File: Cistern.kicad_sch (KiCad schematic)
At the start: 16 parts, among them J2 Gauge Stepper, J3 Power Connector, Q1 BD244C, Q2 Gauge Calibration, SW1 WiFi reset, SW2 Water Sensor, U1 ULN2003A, U3 Boost Converter (5->20 V)

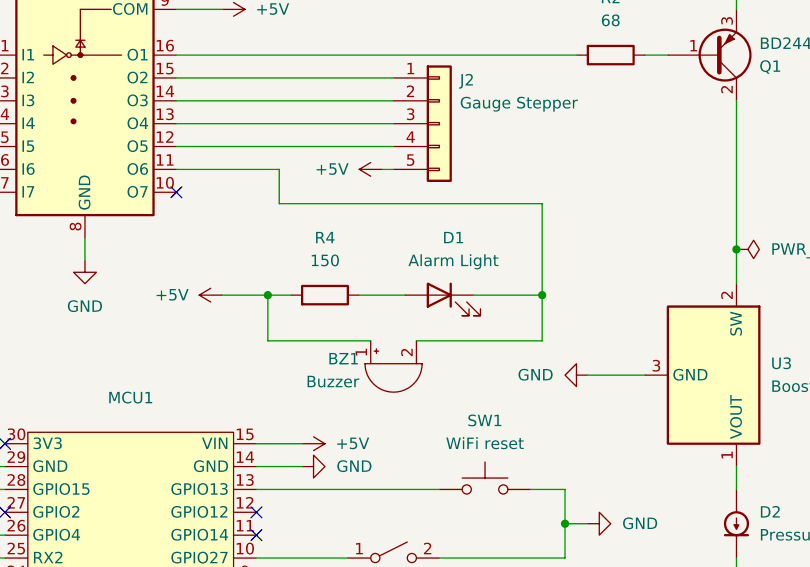
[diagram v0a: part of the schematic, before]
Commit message: Improving design some more, fixing custom footprints
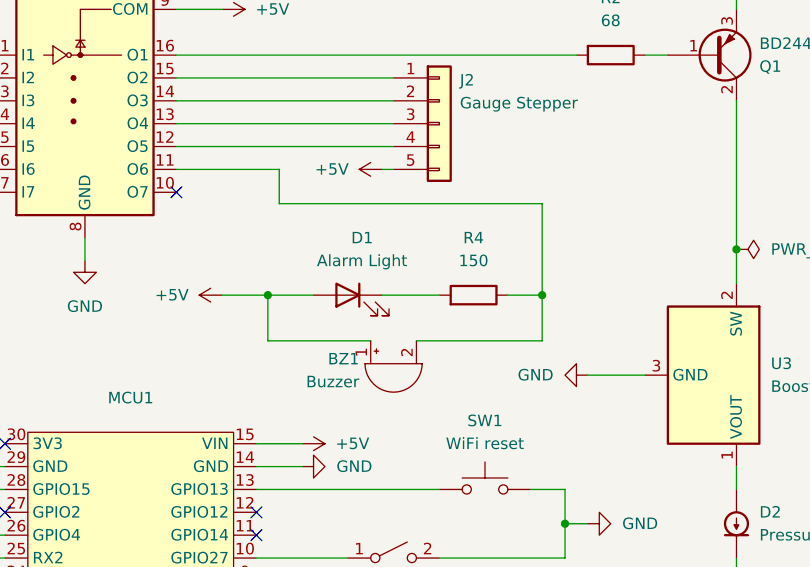
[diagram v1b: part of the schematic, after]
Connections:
- net +5V: now also D1.2 (A); no longer R4.2
- net at BZ1.2 (-), U1.11 (O6): now also R4.1; no longer D1.1 (K)
- new net: D1.1 (K), R4.2
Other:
- moved on the sheet: D1, R4
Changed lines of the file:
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@@
+	)
+	(junction
+		(at 59.69 160.02)
+		(diameter 0)
+		(color 0 0 0 0)
+	)
+	(junction
+		(at 228.6 110.49)
+		(diameter 0)
+		(color 0 0 0 0)
 	)
 	(junction
@@
 	)
 	(junction
-		(at 59.69 160.02)
-		(diameter 0)
-		(color 0 0 0 0)
-	)
-	(junction
-		(at 228.6 110.49)
-		(diameter 0)
-		(color 0 0 0 0)
-	)
-	(junction
 		(at 223.52 120.65)
 		(diameter 0)
@@
 	(wire
 		(pts
-			(xy 207.01 78.74) (xy 207.01 73.66)
-		)
-		(stroke
-			(width 0)
-			(type default)
-		)
-	)
-	(wire
-		(pts
 			(xy 133.35 95.25) (xy 147.32 95.25)
 		)
@@
 	(wire
 		(pts
+			(xy 176.53 73.66) (xy 181.61 73.66)
+		)
+		(stroke
+			(width 0)
+			(type default)
+		)
+	)
+	(wire
+		(pts
 			(xy 209.55 99.06) (xy 212.09 99.06)
 		)
@@
 	(wire
 		(pts
-			(xy 199.39 73.66) (xy 207.01 73.66)
-		)
-		(stroke
-			(width 0)
-			(type default)
-		)
-	)
-	(wire
-		(pts
 			(xy 228.6 120.65) (xy 228.6 119.38)
 		)
@@
 	(wire
 		(pts
-			(xy 176.53 78.74) (xy 176.53 73.66)
+			(xy 176.53 73.66) (xy 176.53 78.74)
 		)
 		(stroke
@@
 	(wire
 		(pts
+			(xy 207.01 73.66) (xy 207.01 78.74)
+		)
+		(stroke
+			(width 0)
+			(type default)
+		)
+	)
+	(wire
+		(pts
 			(xy 187.96 78.74) (xy 176.53 78.74)
 		)
@@
 	(wire
 		(pts
+			(xy 203.2 73.66) (xy 207.01 73.66)
+		)
+		(stroke
+			(width 0)
+			(type default)
+		)
+	)
+	(wire
+		(pts
 			(xy 134.62 123.19) (xy 147.32 123.19)
 		)
@@
 	(wire
 		(pts
-			(xy 176.53 73.66) (xy 179.07 73.66)
-		)
-		(stroke
-			(width 0)
-			(type default)
-		)
-	)
-	(wire
-		(pts
 			(xy 59.69 156.21) (xy 59.69 160.02)
 		)
@@
 	(wire
 		(pts
+			(xy 189.23 73.66) (xy 195.58 73.66)
+		)
+		(stroke
+			(width 0)
+			(type default)
+		)
+	)
+	(wire
+		(pts
 			(xy 193.04 78.74) (xy 207.01 78.74)
-		)
-		(stroke
-			(width 0)
-			(type default)
-		)
-	)
-	(wire
-		(pts
-			(xy 191.77 73.66) (xy 186.69 73.66)
 		)
 		(stroke
@@
 	(symbol
 		(lib_id "Device:LED")
-		(at 195.58 73.66 0)
+		(at 185.42 73.66 0)
 		(mirror y)
 		(unit 1)
@@
 		(dnp no)
 		(property "Reference" "D1"
-			(at 197.1675 67.31 0)
+			(at 187.0075 67.31 0)
 			(effects
 				(font
@@
 		)
 		(property "Value" "Alarm Light"
-			(at 197.1675 69.85 0)
+			(at 187.0075 69.85 0)
 			(effects
 				(font
@@
 		)
 		(property "Footprint" "LED_THT:LED_D5.0mm"
-			(at 195.58 73.66 0)
+			(at 185.42 73.66 0)
 			(effects
 				(font
@@
 		)
 		(property "Datasheet" "~"
-			(at 195.58 73.66 0)
+			(at 185.42 73.66 0)
 			(effects
 				(font
@@
 		)
 		(property "Description" "Light emitting diode"
-			(at 195.58 73.66 0)
+			(at 185.42 73.66 0)
 			(effects
 				(font
@@
 	(symbol
 		(lib_id "Device:R")
-		(at 182.88 73.66 270)
+		(at 199.39 73.66 270)
 		(mirror x)
 		(unit 1)
@@
 		(fields_autoplaced yes)
 		(property "Reference" "R4"
-			(at 182.88 67.31 90)
+			(at 199.39 67.31 90)
 			(effects
 				(font
@@
 		)
 		(property "Value" "150"
-			(at 182.88 69.85 90)
+			(at 199.39 69.85 90)
 			(effects
 				(font
@@
 		)
 		(property "Footprint" "Resistor_THT:R_Axial_DIN0207_L6.3mm_D2.5mm_P7.62mm_Horizontal"
-			(at 182.88 75.438 90)
+			(at 199.39 75.438 90)
 			(effects
 				(font
@@
 		)
 		(property "Datasheet" "~"
-			(at 182.88 73.66 0)
+			(at 199.39 73.66 0)
 			(effects
 				(font
@@
 		)
 		(property "Description" "Resistor"
-			(at 182.88 73.66 0)
-			(effects
-				(font
+			(at 199.39 73.66 0)
+			(effects
+				(font

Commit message: Replacing individual pins with GPIO header
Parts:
- removed Q2: Gauge Calibration, Connector_PinHeader_2.54mm:PinHeader_1x02_P2.54mm_Vertical, symbol Device:Q_Photo_NPN
- removed SW2: Water Sensor, Connector_PinHeader_2.54mm:PinHeader_1x02_P2.54mm_Vertical, symbol Switch:SW_SPST
- added J1: GPIO, Connector_PinHeader_2.54mm:PinHeader_1x06_P2.54mm_Vertical, symbol Connector_Generic:Conn_01x06
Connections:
- net at MCU1.10 (GPIO27): now also J1.2 (Pin_2)
- net at MCU1.11 (GPIO14): now also J1.1 (Pin_1)
- net at MCU1.4 (GPIO34): now also D2.1 (K), D3.1 (K), R1.1
- net at MCU1.6 (GPIO32): now also J1.6 (Pin_6)
- net at MCU1.8 (GPIO25): now also J1.4 (Pin_4)
- net at MCU1.9 (GPIO26): now also J1.3 (Pin_3)
- new net: J1.5 (Pin_5), MCU1.7 (GPIO33)
- no-connect marks 19 -> 15

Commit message: Adding GND header
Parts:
- added J4: GND, Connector_PinHeader_2.54mm:PinHeader_1x03_P2.54mm_Vertical, symbol Connector_Generic:Conn_01x03
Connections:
- net GND: now also J4.1 (Pin_1), J4.2 (Pin_2), J4.3 (Pin_3)
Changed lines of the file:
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@@
+	)
+	(junction
+		(at 64.77 73.66)
+		(diameter 0)
+		(color 0 0 0 0)
 	)
 	(junction
@@
 	)
 	(junction
+		(at 64.77 71.12)
+		(diameter 0)
+		(color 0 0 0 0)
+	)
+	(junction
 		(at 176.53 73.66)
 		(diameter 0)
@@
 	(wire
 		(pts
+			(xy 64.77 68.58) (xy 68.58 68.58)
+		)
+		(stroke
+			(width 0)
+			(type default)
+		)
+	)
+	(wire
+		(pts
 			(xy 212.09 110.49) (xy 218.44 110.49)
 		)
@@
 	(wire
 		(pts
+			(xy 64.77 73.66) (xy 64.77 71.12)
+		)
+		(stroke
+			(width 0)
+			(type default)
+		)
+	)
+	(wire
+		(pts
 			(xy 123.19 49.53) (xy 123.19 110.49)
 		)
@@
 	(wire
 		(pts
+			(xy 64.77 71.12) (xy 68.58 71.12)
+		)
+		(stroke
+			(width 0)
+			(type default)
+		)
+	)
+	(wire
+		(pts
 			(xy 189.23 102.87) (xy 175.26 102.87)
 		)
@@
 	(wire
 		(pts
+			(xy 64.77 73.66) (xy 68.58 73.66)
+		)
+		(stroke
+			(width 0)
+			(type default)
+		)
+	)
+	(wire
+		(pts
 			(xy 177.8 63.5) (xy 207.01 63.5)
 		)
@@
 	(wire
 		(pts
+			(xy 64.77 76.2) (xy 64.77 73.66)
+		)
+		(stroke
+			(width 0)
+			(type default)
+		)
+	)
+	(wire
+		(pts
 			(xy 166.37 57.15) (xy 190.5 57.15)
+		)
+		(stroke
+			(width 0)
+			(type default)
+		)
+	)
+	(wire
+		(pts
+			(xy 64.77 71.12) (xy 64.77 68.58)
 		)
 		(stroke
@@
 				(path "/387a1b1b-4d04-4a4f-a341-bb26b6058549"
 					(reference "#PWR03")
+					(unit 1)
+				)
+			)
+		)
+	)
+	(symbol
+		(lib_id "Connector_Generic:Conn_01x03")
+		(at 73.66 71.12 0)
+		(unit 1)
+		(exclude_from_sim no)
+		(in_bom yes)
+		(on_board yes)
+		(dnp no)
+		(fields_autoplaced yes)
+		(property "Reference" "J4"
+			(at 76.2 69.8499 0)
+			(effects
+				(font
+					(size 1.27 1.27)
+				)
+				(justify left)
+			)
+		)
+		(property "Value" "GND"
+			(at 76.2 72.3899 0)
+			(effects
+				(font
+					(size 1.27 1.27)
+				)
+				(justify left)
+			)
+		)
+		(property "Footprint" "Connector_PinHeader_2.54mm:PinHeader_1x03_P2.54mm_Vertical"
+			(at 73.66 71.12 0)
+			(effects
+				(font
+					(size 1.27 1.27)
+				)
+				(hide yes)
+			)
+		)
+		(property "Datasheet" "~"
+			(at 73.66 71.12 0)
+			(effects
+				(font
+					(size 1.27 1.27)
+				)
+				(hide yes)
+			)
+		)
+		(property "Description" "Generic connector, single row, 01x03, script generated (kicad-library-utils/schlib/autogen/connector/)"
+			(at 73.66 71.12 0)
+			(effects
+				(font
+					(size 1.27 1.27)
+				)
+				(hide yes)
+			)
+		)
+		(pin "1"
+		)
+		(pin "2"
+		)
+		(pin "3"
+		)
+		(instances
+			(project ""
+				(path "/387a1b1b-4d04-4a4f-a341-bb26b6058549"
+					(reference "J4")
 					(unit 1)
 				)
@@
 					(unit 1)
 				)
+			)
+		)
+	)
+	(symbol
+		(lib_id "power:GND")
+		(at 64.77 76.2 0)
+		(unit 1)
+		(exclude_from_sim no)
+		(in_bom yes)
+		(on_board yes)
+		(dnp no)
+		(fields_autoplaced yes)
+		(property "Reference" "#PWR09"
+			(at 64.77 82.55 0)
+			(effects
+				(font
+					(size 1.27 1.27)
+				)
+				(hide yes)
+			)
+		)
+		(property "Value" "GND"
+			(at 64.77 81.28 0)
+			(effects
+				(font
+					(size 1.27 1.27)
+				)
+			)
+		)
+		(property "Footprint" ""
+			(at 64.77 76.2 0)
+			(effects
+				(font
+					(size 1.27 1.27)
+				)
+				(hide yes)
+			)
+		)
+		(property "Datasheet" ""
+			(at 64.77 76.2 0)
+			(effects
+				(font
+					(size 1.27 1.27)
+				)
+				(hide yes)
+			)
+		)
+		(property "Description" "Power symbol creates a global label with name \"GND\" , ground"
+			(at 64.77 76.2 0)
+			(effects
+				(font
+					(size 1.27 1.27)
+				)
+				(hide yes)
+			)
+		)
+		(pin "1"
+		)
+		(instances
+			(project ""
+				(path "/387a1b1b-4d04-4a4f-a341-bb26b6058549"
+					(reference "#PWR09")
+					(unit 1)
+				)
